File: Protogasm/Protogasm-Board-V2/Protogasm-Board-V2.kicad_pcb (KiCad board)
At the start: 2 copper layers, 68.6 x 53.3 mm, 10 parts, among them J1 Neopixel_Ring_Header, M1 Motor_DC, Q1 FQP30N06L, SW1 Rotary_Encoder_Switch, U1 Arduino_UNO_R3, U2 MPX5050GP

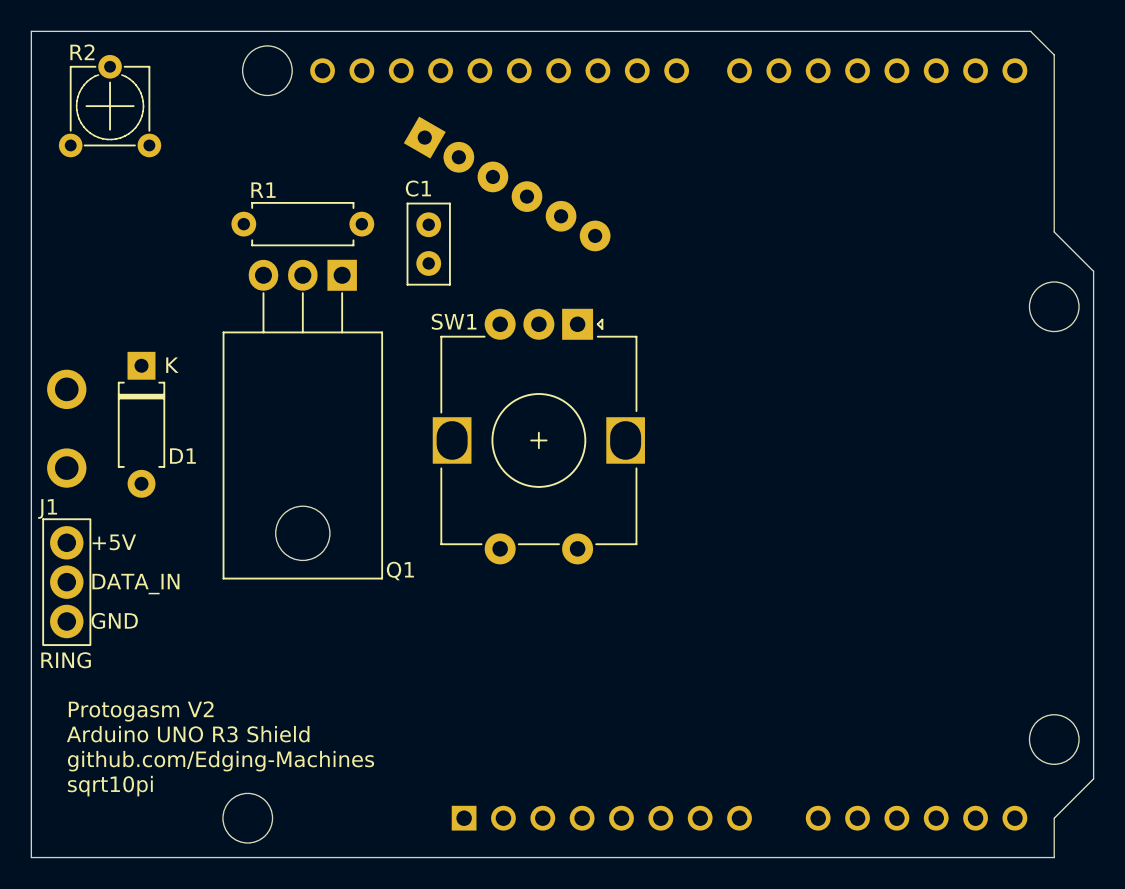
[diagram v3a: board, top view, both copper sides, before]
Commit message: Finalize Protogasm-Board-V3, with properly placed MPX and SW1
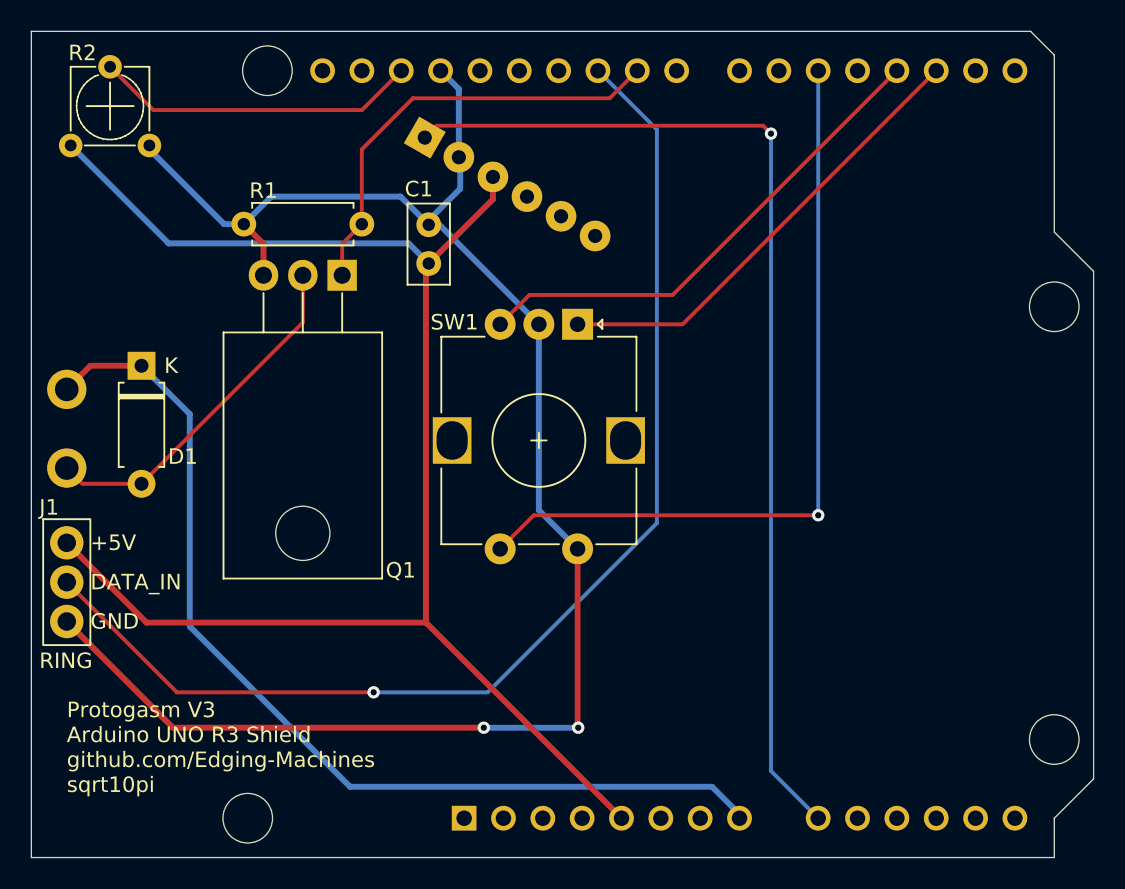
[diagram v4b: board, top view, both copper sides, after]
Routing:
- net GND: track 0.00 -> 109.6 mm, vias 0 -> 2
- net +5V: track 0.00 -> 100.0 mm
- net /D10: track 0.00 -> 76.4 mm, vias 0 -> 1
- net /A0: track 0.00 -> 68.3 mm, vias 0 -> 1
- net +12V: track 0.00 -> 64.3 mm
- net /D5: track 0.00 -> 50.1 mm, vias 0 -> 1
- net /D3: track 0.00 -> 32.4 mm
- net /D2: track 0.00 -> 29.9 mm
- net /D9: track 0.00 -> 28.5 mm
- net /MOTOR-: track 0.00 -> 23.0 mm
- net /AREF: track 0.00 -> 21.0 mm
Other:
- board text added: "Protogasm V3 Arduino UNO R3 Shield github.com/Edging-Machines sqrt10pi"
- board text removed: "Protogasm V2 Arduino UNO R3 Shield github.com/Edging-Machines sqrt10pi"
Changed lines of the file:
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@@
       (effects (font (size 1 1) (thickness 0.15)))
     )
-    (fp_text value "FQP30N06L" (at 2.54 2) (layer "F.Fab")
+    (fp_text value "FQP30N06L" (at 2.54 -4.826) (layer "F.Fab")
       (effects (font (size 1 1) (thickness 0.15)))
     )
@@
       (effects (font (size 1 1) (thickness 0.15)))
     )
-    (fp_text value "1N5818-B" (at 3.81 2.47 90) (layer "F.Fab")
+    (fp_text value "1N5818-B" (at 5.08 -2.286 90) (layer "F.Fab")
       (effects (font (size 1 1) (thickness 0.15)))
     )
@@
   (gr_rect (start 176.784 91.44) (end 171.196 100.838) (layer "User.1") (width 0.15) (fill none))
   (gr_rect (start 121.92 101.092) (end 133.096 95.504) (layer "User.2") (width 0.15) (fill none))
-  (gr_text "Protogasm V2\nArduino UNO R3 Shield\ngithub.com/Edging-Machines\nsqrt10pi" (at 111.506 117.348) (layer "F.SilkS")
+  (gr_text "Protogasm V3\nArduino UNO R3 Shield\ngithub.com/Edging-Machines\nsqrt10pi" (at 111.506 117.348) (layer "F.SilkS")
     (effects (font (size 1 1) (thickness 0.15)) (justify left))
   )
@@
   )
   (target plus (at 177.8 124.46) (size 5) (width 0.05) (layer "Edge.Cuts"))
+  (segment (start 134.874 86.106) (end 139.019409 81.960591) (width 0.381) (layer "F.Cu") (net 1))
+  (segment (start 139.019409 81.960591) (end 139.019409 80.518) (width 0.381) (layer "F.Cu") (net 1))
+  (segment (start 134.691989 86.288011) (end 134.874 86.106) (width 0.381) (layer "F.Cu") (net 1))
+  (segment (start 147.32 121.92) (end 134.691989 109.291989) (width 0.381) (layer "F.Cu") (net 1))
+  (segment (start 134.691989 109.291989) (end 134.691989 86.288011) (width 0.381) (layer "F.Cu") (net 1))
+  (segment (start 111.506 104.14) (end 116.657989 109.291989) (width 0.381) (layer "F.Cu") (net 1))
+  (segment (start 116.657989 109.291989) (end 134.691989 109.291989) (width 0.381) (layer "F.Cu") (net 1))
+  (segment (start 118.084011 84.810011) (end 133.578011 84.810011) (width 0.381) (layer "B.Cu") (net 1))
+  (segment (start 133.578011 84.810011) (end 134.874 86.106) (width 0.381) (layer "B.Cu") (net 1))
+  (segment (start 111.76 78.486) (end 118.084011 84.810011) (width 0.381) (layer "B.Cu") (net 1))
+  (segment (start 144.486 116.038) (end 144.526 116.078) (width 0.381) (layer "F.Cu") (net 2))
+  (segment (start 124.206 86.868) (end 124.206 84.836) (width 0.381) (layer "F.Cu") (net 2))
+  (segment (start 118.364 116.078) (end 138.43 116.078) (width 0.381) (layer "F.Cu") (net 2))
+  (segment (start 144.486 104.532) (end 144.486 116.038) (width 0.381) (layer "F.Cu") (net 2))
+  (segment (start 111.506 109.22) (end 118.364 116.078) (width 0.381) (layer "F.Cu") (net 2))
+  (segment (start 124.206 84.836) (end 122.936 83.566) (width 0.381) (layer "F.Cu") (net 2))
+  (via (at 138.43 116.078) (size 0.8) (drill 0.4) (layers "F.Cu" "B.Cu") (free) (net 2))
+  (via (at 144.526 116.078) (size 0.8) (drill 0.4) (layers "F.Cu" "B.Cu") (free) (net 2))
+  (segment (start 136.906 79.334295) (end 136.819705 79.248) (width 0.381) (layer "B.Cu") (net 2))
+  (segment (start 116.84 78.74) (end 116.84 78.486) (width 0.381) (layer "B.Cu") (net 2))
+  (segment (start 124.714 81.788) (end 122.936 83.566) (width 0.381) (layer "B.Cu") (net 2))
+  (segment (start 136.906 81.28) (end 136.906 79.334295) (width 0.381) (layer "B.Cu") (net 2))
+  (segment (start 136.819705 74.839705) (end 135.64 73.66) (width 0.381) (layer "B.Cu") (net 2))
+  (segment (start 133.056 81.788) (end 124.714 81.788) (width 0.381) (layer "B.Cu") (net 2))
+  (segment (start 141.986 102.032) (end 141.986 90.032) (width 0.381) (layer "B.Cu") (net 2))
+  (segment (start 134.874 83.606) (end 135.56 83.606) (width 0.381) (layer "B.Cu") (net 2))
+  (segment (start 134.874 83.312) (end 136.906 81.28) (width 0.381) (layer "B.Cu") (net 2))
+  (segment (start 134.874 83.606) (end 134.874 83.312) (width 0.381) (layer "B.Cu") (net 2))
+  (segment (start 135.56 83.606) (end 141.986 90.032) (width 0.381) (layer "B.Cu") (net 2))
+  (segment (start 144.486 104.532) (end 141.986 102.032) (width 0.381) (layer "B.Cu") (net 2))
+  (segment (start 144.526 116.078) (end 138.43 116.078) (width 0.381) (layer "B.Cu") (net 2))
+  (segment (start 121.666 83.566) (end 116.84 78.74) (width 0.381) (layer "B.Cu") (net 2))
+  (segment (start 136.819705 79.248) (end 136.819705 74.839705) (width 0.381) (layer "B.Cu") (net 2))
+  (segment (start 122.936 83.566) (end 121.666 83.566) (width 0.381) (layer "B.Cu") (net 2))
+  (segment (start 134.874 83.606) (end 133.056 81.788) (width 0.381) (layer "B.Cu") (net 2))
+  (segment (start 113.03 92.71) (end 111.506 94.234) (width 0.381) (layer "F.Cu") (net 3))
+  (segment (start 116.332 92.71) (end 113.03 92.71) (width 0.381) (layer "F.Cu") (net 3))
+  (segment (start 129.794 119.888) (end 153.162 119.888) (width 0.381) (layer "B.Cu") (net 3))
+  (segment (start 116.332 92.71) (end 119.448558 95.826558) (width 0.381) (layer "B.Cu") (net 3))
+  (segment (start 119.448558 95.826558) (end 119.448558 109.542558) (width 0.381) (layer "B.Cu") (net 3))
+  (segment (start 119.448558 109.542558) (end 129.794 119.888) (width 0.381) (layer "B.Cu") (net 3))
+  (segment (start 153.162 119.888) (end 154.94 121.666) (width 0.381) (layer "B.Cu") (net 3))
+  (segment (start 154.94 121.666) (end 154.94 121.92) (width 0.381) (layer "B.Cu") (net 3))
+  (segment (start 112.522 100.33) (end 116.332 100.33) (width 0.25) (layer "F.Cu") (net 4))
+  (segment (start 111.506 99.314) (end 112.522 100.33) (width 0.25) (layer "F.Cu") (net 4))
+  (segment (start 126.746 86.868) (end 126.746 89.916) (width 0.25) (layer "F.Cu") (net 4))
+  (segment (start 126.746 89.916) (end 116.332 100.33) (width 0.25) (layer "F.Cu") (net 4))
+  (segment (start 118.618 113.792) (end 111.506 106.68) (width 0.25) (layer "F.Cu") (net 5))
+  (segment (start 131.318 113.792) (end 118.618 113.792) (width 0.25) (layer "F.Cu") (net 5))
+  (via (at 131.318 113.792) (size 0.8) (drill 0.4) (layers "F.Cu" "B.Cu") (free) (net 5))
+  (segment (start 145.8 73.66) (end 149.606 77.466) (width 0.25) (layer "B.Cu") (net 5))
+  (segment (start 149.606 102.87) (end 138.684 113.792) (width 0.25) (layer "B.Cu") (net 5))
+  (segment (start 149.606 77.466) (end 149.606 102.87) (width 0.25) (layer "B.Cu") (net 5))
+  (segment (start 138.684 113.792) (end 131.318 113.792) (width 0.25) (layer "B.Cu") (net 5))
+  (segment (start 146.562 75.438) (end 148.34 73.66) (width 0.25) (layer "F.Cu") (net 6))
+  (segment (start 133.858 75.438) (end 146.562 75.438) (width 0.25) (layer "F.Cu") (net 6))
+  (segment (start 130.556 78.74) (end 133.858 75.438) (width 0.25) (layer "F.Cu") (net 6))
+  (segment (start 129.286 86.868) (end 129.286 84.836) (width 0.25) (layer "F.Cu") (net 6))
+  (segment (start 129.286 84.836) (end 130.556 83.566) (width 0.25) (layer "F.Cu") (net 6))
+  (segment (start 130.556 83.566) (end 130.556 78.74) (width 0.25) (layer "F.Cu") (net 6))
+  (segment (start 130.56 76.2) (end 133.1 73.66) (width 0.25) (layer "F.Cu") (net 7))
+  (segment (start 117.094 76.2) (end 130.56 76.2) (width 0.25) (layer "F.Cu") (net 7))
+  (segment (start 114.3 73.406) (end 117.094 76.2) (width 0.25) (layer "F.Cu") (net 7))
+  (segment (start 151.268 90.032) (end 167.64 73.66) (width 0.25) (layer "F.Cu") (net 8))
+  (segment (start 144.486 90.032) (end 151.268 90.032) (width 0.25) (layer "F.Cu") (net 8))
+  (segment (start 150.622 88.138) (end 165.1 73.66) (width 0.25) (layer "F.Cu") (net 9))
+  (segment (start 141.38 88.138) (end 150.622 88.138) (width 0.25) (layer "F.Cu") (net 9))
+  (segment (start 139.486 90.032) (end 141.38 88.138) (width 0.25) (layer "F.Cu") (net 9))
+  (segment (start 141.656 102.362) (end 160.02 102.362) (width 0.25) (layer "F.Cu") (net 10))
+  (segment (start 139.486 104.532) (end 141.656 102.362) (width 0.25) (layer "F.Cu") (net 10))
+  (via (at 160.02 102.362) (size 0.8) (drill 0.4) (layers "F.Cu" "B.Cu") (free) (net 10))
+  (segment (start 160.02 73.66) (end 160.02 102.362) (width 0.25) (layer "B.Cu") (net 10))
+  (segment (start 156.464 77.216) (end 135.382 77.216) (width 0.25) (layer "F.Cu") (net 23))
+  (segment (start 135.382 77.216) (end 134.62 77.978) (width 0.25) (layer "F.Cu") (net 23))
+  (segment (start 156.972 77.724) (end 156.464 77.216) (width 0.25) (layer "F.Cu") (net 23))
+  (via (at 156.972 77.724) (size 0.8) (drill 0.4) (layers "F.Cu" "B.Cu") (free) (net 23))
+  (segment (start 156.972 118.872) (end 156.972 77.724) (width 0.25) (layer "B.Cu") (net 23))
+  (segment (start 160.02 121.92) (end 156.972 118.872) (width 0.25) (layer "B.Cu") (net 23))
 )

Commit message: Protogasm V4 - with DCDC converter and dedicated power jack
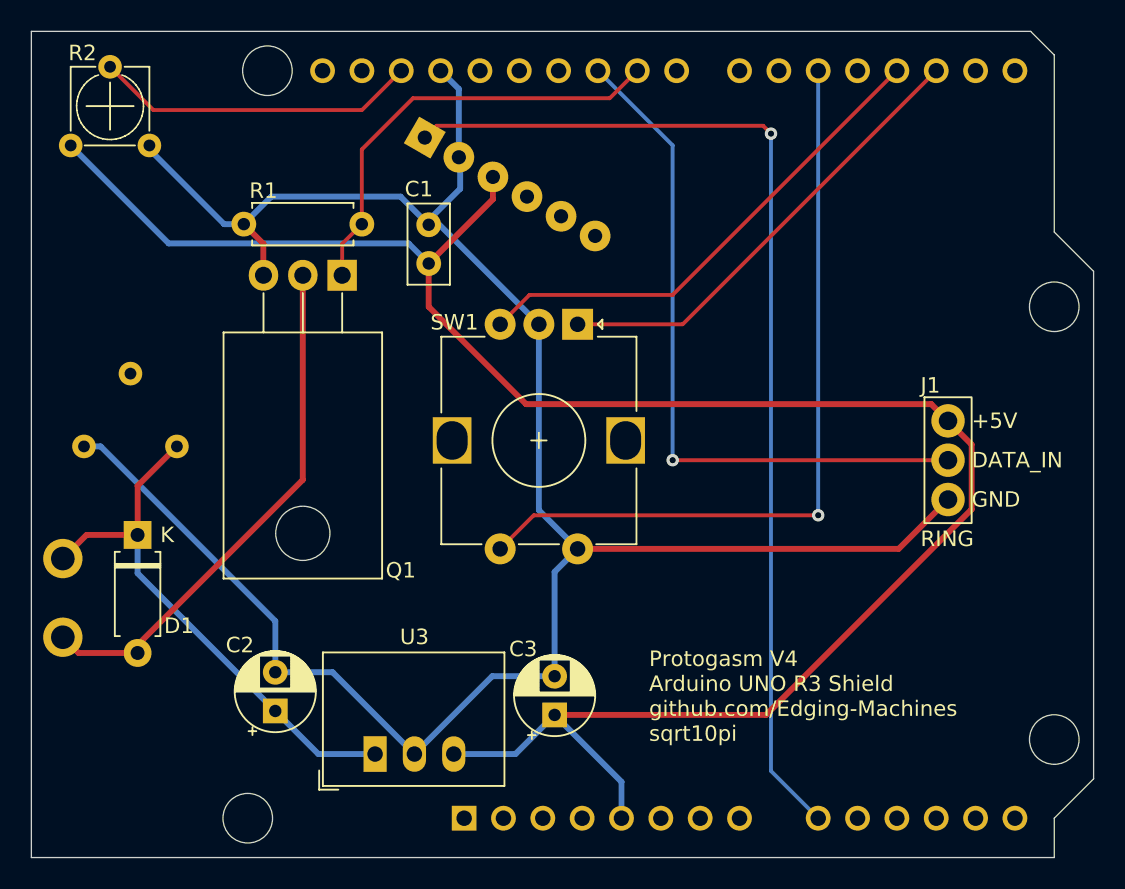
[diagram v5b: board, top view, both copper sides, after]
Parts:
- added C2: 10u, Capacitor_THT:CP_Radial_D5.0mm_P2.50mm, F.Cu at (125.0, 115.0)
- added C3: 10u, Capacitor_THT:CP_Radial_D5.0mm_P2.50mm, F.Cu at (143.0, 115.3)
- added J2: Jack-DC, custom-footprints:2.1mm DC Barrel Jack, B.Cu at (118.6, 97.9)
- added U3: R-78E5.0-0.5, Converter_DCDC:Converter_DCDC_RECOM_R-78E-0.5_THT, F.Cu at (131.4, 117.8)
- moved J1 57.4 mm to (168.4, 96.3)
- moved D1 10.9 mm to (116.1, 103.6)
- moved M1 10.9 mm to (111.3, 105.2)
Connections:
- U1 pad 8: +12V -> unconnected-(U1-Pad8)
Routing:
- net /D10: track 76.4 -> 44.9 mm
- net +12V: track 64.3 -> 34.9 mm
- net GND: track 109.6 -> 138.9 mm, vias 2 -> 0
- net +5V: track 100.0 -> 127.7 mm
- net /MOTOR-: track 23.0 -> 34.0 mm
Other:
- board text added: "Protogasm V4 Arduino UNO R3 Shield github.com/Edging-Machines sqrt10pi"
- board text removed: "Protogasm V3 Arduino UNO R3 Shield github.com/Edging-Machines sqrt10pi"
